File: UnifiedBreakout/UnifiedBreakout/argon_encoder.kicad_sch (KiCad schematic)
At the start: 3 parts, among them J12 ENCODER IN, J13 ENCODER OUT

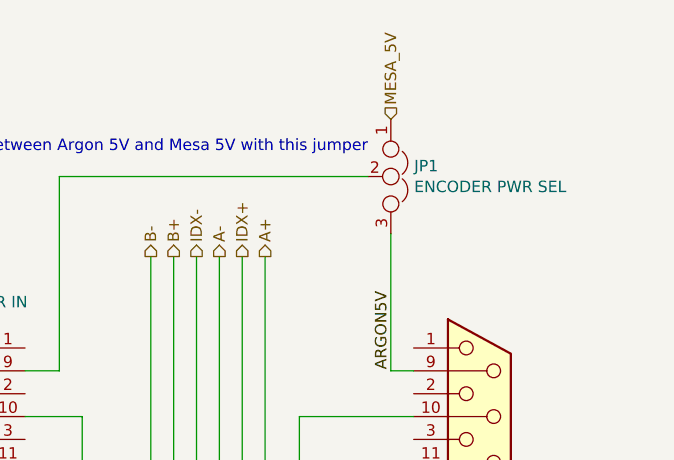
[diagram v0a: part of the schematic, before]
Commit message: Upgrade to new KiCAD version
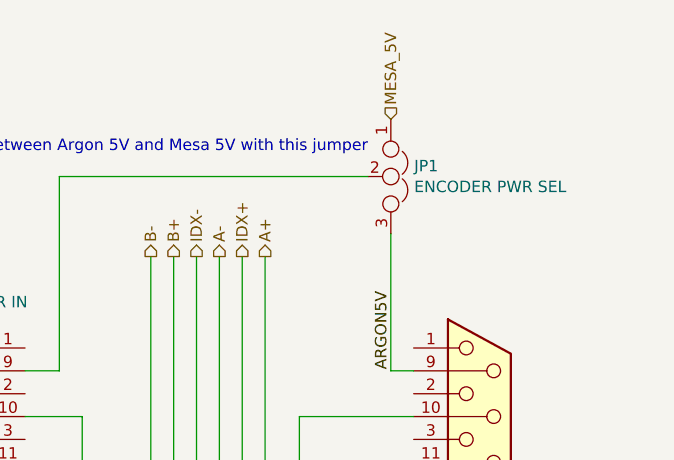
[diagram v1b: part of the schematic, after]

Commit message: WIP updating breakout for electrical enclosure
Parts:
- removed JP1: ENCODER PWR SEL, Connector_PinHeader_2.54mm:PinHeader_1x03_P2.54mm_Vertical, symbol UnifiedBreakout-rescue:Jumper_NC_Dual-Device
- J12, J13: symbol UnifiedBreakout-rescue:DB15_Female_MountingHoles-Connector -> Connector:DA15_Receptacle
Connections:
- net ARGON5V is gone; now on an unnamed net: J13.9 (P9)
- net GND: no longer J12.0 (PAD), J13.0 (PAD)
- no-connect marks 0 -> 14
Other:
- note added: "Encoder powered by Argon"
- note removed: "Select between Argon 5V and Mesa 5V with this jumper"

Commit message: Add stacked DA15 part
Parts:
- removed J12: ENCODER IN, Connector_Dsub:DSUB-15_Female_Horizontal_P2.77x2.84mm_EdgePinOffset7.70mm_Housed_MountingHolesOffset9.12mm, symbol Connector:DA15_Receptacle
- removed J13: ENCODER OUT, Connector_Dsub:DSUB-15_Female_Horizontal_P2.77x2.84mm_EdgePinOffset7.70mm_Housed_MountingHolesOffset9.12mm, symbol Connector:DA15_Receptacle
- added J3: Dual DA15 Stacked, UnifiedBreakout:NorComp-Dual-DA15, symbol UnifiedBreakout:DA15_Receptacle_Dual
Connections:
- net A+: now also J3.A8, J3.B8
- net A-: now also J3.A7, J3.B7
- net B+: now also J3.A6, J3.B6
- net B-: now also J3.A5, J3.B5
- net GND: now also J3.A10, J3.B10, J3.MH1, J3.MH2, J3.MH3, J3.MH4
- net IDX+: now also J3.A15, J3.B15
- net IDX-: now also J3.A14, J3.B14
- new net: J3.A9, J3.B9
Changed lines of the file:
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@@
   (junction (at 130.81 106.68) (diameter 0.9144) (color 0 0 0 0)
+  )
+  (junction (at 96.52 114.3) (diameter 0) (color 0 0 0 0)
   )
   (junction (at 125.73 101.6) (diameter 0.9144) (color 0 0 0 0)
@@
     (stroke (width 0) (type solid))
   )
+  (wire (pts (xy 93.98 114.3) (xy 96.52 114.3))
+    (stroke (width 0) (type default))
+  )
   (wire (pts (xy 110.49 114.3) (xy 96.52 114.3))
     (stroke (width 0) (type solid))
@@
     (stroke (width 0) (type solid))
   )
+  (wire (pts (xy 157.48 111.76) (xy 157.48 114.3))
+    (stroke (width 0) (type default))
+  )
   (wire (pts (xy 104.14 101.6) (xy 125.73 101.6))
     (stroke (width 0) (type solid))
   )
+  (wire (pts (xy 157.48 114.3) (xy 154.94 114.3))
+    (stroke (width 0) (type default))
+  )
   (wire (pts (xy 118.11 91.44) (xy 118.11 60.96))
     (stroke (width 0) (type solid))
@@
   (wire (pts (xy 147.32 104.14) (xy 128.27 104.14))
     (stroke (width 0) (type solid))
+  )
+  (wire (pts (xy 93.98 111.76) (xy 93.98 114.3))
+    (stroke (width 0) (type default))
   )
   (wire (pts (xy 104.14 78.74) (xy 110.49 78.74))
@@
     (effects (font (size 1.27 1.27)) (justify left))
   )
-  (symbol (lib_id "Connector:DA15_Receptacle") (at 154.94 88.9 0) (unit 1)
-    (in_bom yes) (on_board yes) (dnp no)
-    (property "Reference" "J13" (at 158.8516 88.8492 0)
-      (effects (font (size 1.27 1.27)) (justify left))
-    )
-    (property "Value" "ENCODER OUT" (at 158.8516 91.1606 0)
-      (effects (font (size 1.27 1.27)) (justify left))
-    )
-    (property "Footprint" "Connector_Dsub:DSUB-15_Female_Horizontal_P2.77x2.84mm_EdgePinOffset7.70mm_Housed_MountingHolesOffset9.12mm" (at 154.94 88.9 0)
+  (symbol (lib_id "UnifiedBreakout:DA15_Receptacle_Dual") (at 154.94 88.9 0) (unit 2)
+    (in_bom yes) (on_board yes) (dnp no) (fields_autoplaced)
+    (property "Reference" "J3" (at 160.02 84.455 0)
+      (effects (font (size 1.27 1.27)) (justify left))
+    )
+    (property "Value" "Dual DA15 Stacked" (at 160.02 86.995 0)
+      (effects (font (size 1.27 1.27)) (justify left))
+    )
+    (property "Footprint" "UnifiedBreakout:NorComp-Dual-DA15" (at 154.94 88.9 0)
       (effects (font (size 1.27 1.27)) hide)
     )
@@
       (effects (font (size 1.27 1.27)) hide)
     )
-    (property "Farnell PN" "" (at 154.94 88.9 0)
-      (effects (font (size 1.27 1.27)) hide)
-    )
-    (pin "1")
-    (pin "10")
-    (pin "11")
-    (pin "12")
-    (pin "13")
-    (pin "14")
-    (pin "15")
-    (pin "2")
-    (pin "3")
-    (pin "4")
-    (pin "5")
-    (pin "6")
-    (pin "7")
-    (pin "8")
-    (pin "9")
+    (property "Farnell PN" "2294319" (at 160.02 89.535 0)
+      (effects (font (size 1.27 1.27)) (justify left))
+    )
+    (property "MPN" "178-015-513R571" (at 160.02 92.075 0)
+      (effects (font (size 1.27 1.27)) (justify left))
+    )
+    (property "Manufacturer" "NORCOMP" (at 160.02 94.615 0)
+      (effects (font (size 1.27 1.27)) (justify left))
+    )
+    (pin "A1")
+    (pin "A10")
+    (pin "A11")
+    (pin "A12")
+    (pin "A13")
+    (pin "A14")
+    (pin "A15")
+    (pin "A2")
+    (pin "A3")
+    (pin "A4")
+    (pin "A5")
+    (pin "A6")
+    (pin "A7")
+    (pin "A8")
+    (pin "A9")
+    (pin "MH1")
+    (pin "MH2")
+    (pin "")
+    (pin "B1")
+    (pin "B10")
+    (pin "B11")
+    (pin "B12")
+    (pin "B13")
+    (pin "B14")
+    (pin "B15")
+    (pin "B2")
+    (pin "B3")
+    (pin "B4")
+    (pin "B5")
+    (pin "B6")
+    (pin "B7")
+    (pin "B8")
+    (pin "B9")
+    (pin "MH3")
+    (pin "MH4")
     (instances
       (project "UnifiedBreakout"
         (path "/e63e39d7-6ac0-4ffd-8aa3-1841a4541b55/00000000-0000-0000-0000-00005e9de03a"
-          (reference "J13") (unit 1)
+          (reference "J3") (unit 2)
         )
       )
     )
   )
-  (symbol (lib_id "Connector:DA15_Receptacle") (at 96.52 88.9 0) (mirror y) (unit 1)
+  (symbol (lib_id "UnifiedBreakout:DA15_Receptacle_Dual") (at 96.52 88.9 0) (mirror y) (unit 1)
     (in_bom yes) (on_board yes) (dnp no)
-    (property "Reference" "J12" (at 98.9076 63.7032 0)
-      (effects (font (size 1.27 1.27)))
-    )
-    (property "Value" "ENCODER IN" (at 98.9076 66.0146 0)
-      (effects (font (size 1.27 1.27)))
-    )
-    (property "Footprint" "Connector_Dsub:DSUB-15_Female_Horizontal_P2.77x2.84mm_EdgePinOffset7.70mm_Housed_MountingHolesOffset9.12mm" (at 96.52 88.9 0)
+    (property "Reference" "J3" (at 91.44 93.345 0)
+      (effects (font (size 1.27 1.27)) (justify left))
+    )
+    (property "Value" "Dual DA15 Stacked" (at 91.44 90.805 0)
+      (effects (font (size 1.27 1.27)) (justify left))
+    )
+    (property "Footprint" "UnifiedBreakout:NorComp-Dual-DA15" (at 96.52 88.9 0)
       (effects (font (size 1.27 1.27)) hide)
     )
@@
       (effects (font (size 1.27 1.27)) hide)
     )
-    (property "Farnell PN" "" (at 96.52 88.9 0)
-      (effects (font (size 1.27 1.27)) hide)
-    )
-    (pin "1")
-    (pin "10")
-    (pin "11")
-    (pin "12")
-    (pin "13")
-    (pin "14")
-    (pin "15")
-    (pin "2")
-    (pin "3")
-    (pin "4")
-    (pin "5")
-    (pin "6")
-    (pin "7")
-    (pin "8")
-    (pin "9")
+    (property "Farnell PN" "2294319" (at 91.44 88.265 0)
+      (effects (font (size 1.27 1.27)) (justify left))
+    )
+    (property "MPN" "178-015-513R571" (at 91.44 85.725 0)
+      (effects (font (size 1.27 1.27)) (justify left))
+    )
+    (property "Manufacturer" "NORCOMP" (at 91.44 83.185 0)
+      (effects (font (size 1.27 1.27)) (justify left))
+    )
+    (pin "A1")
+    (pin "A10")
+    (pin "A11")
+    (pin "A12")
+    (pin "A13")
+    (pin "A14")
+    (pin "A15")
+    (pin "A2")
+    (pin "A3")
+    (pin "A4")
+    (pin "A5")
+    (pin "A6")
+    (pin "A7")
+    (pin "A8")
+    (pin "A9")
+    (pin "MH1")
+    (pin "MH2")
+    (pin "")
+    (pin "B1")
+    (pin "B10")
+    (pin "B11")
+    (pin "B12")
+    (pin "B13")
+    (pin "B14")
+    (pin "B15")
+    (pin "B2")
+    (pin "B3")
+    (pin "B4")
+    (pin "B5")
+    (pin "B6")
+    (pin "B7")
+    (pin "B8")
+    (pin "B9")
+    (pin "MH3")
+    (pin "MH4")
     (instances
       (project "UnifiedBreakout"
         (path "/e63e39d7-6ac0-4ffd-8aa3-1841a4541b55/00000000-0000-0000-0000-00005e9de03a"
-          (reference "J12") (unit 1)
+          (reference "J3") (unit 1)
         )
       )

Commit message: Update IO and opto
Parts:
- renumbered J3 to J1
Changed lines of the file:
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@@
   (symbol (lib_id "UnifiedBreakout:DA15_Receptacle_Dual") (at 154.94 88.9 0) (unit 2)
     (in_bom yes) (on_board yes) (dnp no) (fields_autoplaced)
-    (property "Reference" "J3" (at 160.02 84.455 0)
+    (property "Reference" "J1" (at 160.02 84.455 0)
       (effects (font (size 1.27 1.27)) (justify left))
     )
@@
       (project "UnifiedBreakout"
         (path "/e63e39d7-6ac0-4ffd-8aa3-1841a4541b55/00000000-0000-0000-0000-00005e9de03a"
-          (reference "J3") (unit 2)
+          (reference "J1") (unit 2)
         )
       )
@@
   (symbol (lib_id "UnifiedBreakout:DA15_Receptacle_Dual") (at 96.52 88.9 0) (mirror y) (unit 1)
     (in_bom yes) (on_board yes) (dnp no)
-    (property "Reference" "J3" (at 91.44 93.345 0)
+    (property "Reference" "J1" (at 91.44 93.345 0)
       (effects (font (size 1.27 1.27)) (justify left))
     )
@@
       (project "UnifiedBreakout"
         (path "/e63e39d7-6ac0-4ffd-8aa3-1841a4541b55/00000000-0000-0000-0000-00005e9de03a"
-          (reference "J3") (unit 1)
+          (reference "J1") (unit 1)
         )
       )

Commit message: Started some layout
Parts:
- removed J1: Dual DA15 Stacked, UnifiedBreakout:NorComp-Dual-DA15, symbol UnifiedBreakout:DA15_Receptacle_Dual
- added J10, J11: DA15_Receptacle_MountingHoles, Connector_Dsub:DSUB-15_Female_Vertical_P2.77x2.84mm_MountingHoles, symbol Connector:DA15_Receptacle_MountingHoles
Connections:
- net A+: now also J10.8, J11.8
- net A-: now also J10.7, J11.7
- net B+: now also J10.6, J11.6
- net B-: now also J10.5, J11.5
- net GND: now also J10.0 (PAD), J10.10 (P10), J11.0 (PAD), J11.10 (P10)
- net IDX+: now also J10.15 (P15), J11.15 (P15)
- net IDX-: now also J10.14 (P14), J11.14 (P14)
- new net: J10.9 (P9), J11.9 (P9)
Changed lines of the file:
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@@
   (junction (at 130.81 106.68) (diameter 0.9144) (color 0 0 0 0)
-  )
-  (junction (at 96.52 114.3) (diameter 0) (color 0 0 0 0)
   )
   (junction (at 125.73 101.6) (diameter 0.9144) (color 0 0 0 0)
@@
     (stroke (width 0) (type solid))
   )
-  (wire (pts (xy 93.98 114.3) (xy 96.52 114.3))
-    (stroke (width 0) (type default))
-  )
   (wire (pts (xy 110.49 114.3) (xy 96.52 114.3))
     (stroke (width 0) (type solid))
@@
     (stroke (width 0) (type solid))
   )
-  (wire (pts (xy 157.48 111.76) (xy 157.48 114.3))
-    (stroke (width 0) (type default))
-  )
   (wire (pts (xy 104.14 101.6) (xy 125.73 101.6))
     (stroke (width 0) (type solid))
   )
-  (wire (pts (xy 157.48 114.3) (xy 154.94 114.3))
-    (stroke (width 0) (type default))
-  )
   (wire (pts (xy 118.11 91.44) (xy 118.11 60.96))
     (stroke (width 0) (type solid))
@@
   (wire (pts (xy 147.32 104.14) (xy 128.27 104.14))
     (stroke (width 0) (type solid))
-  )
-  (wire (pts (xy 93.98 111.76) (xy 93.98 114.3))
-    (stroke (width 0) (type default))
   )
   (wire (pts (xy 104.14 78.74) (xy 110.49 78.74))
@@
     (effects (font (size 1.27 1.27)) (justify left))
   )
-  (symbol (lib_id "UnifiedBreakout:DA15_Receptacle_Dual") (at 154.94 88.9 0) (unit 2)
+  (symbol (lib_id "Connector:DA15_Receptacle_MountingHoles") (at 154.94 88.9 0) (unit 1)
     (in_bom yes) (on_board yes) (dnp no) (fields_autoplaced)
-    (property "Reference" "J1" (at 160.02 84.455 0)
-      (effects (font (size 1.27 1.27)) (justify left))
-    )
-    (property "Value" "Dual DA15 Stacked" (at 160.02 86.995 0)
-      (effects (font (size 1.27 1.27)) (justify left))
-    )
-    (property "Footprint" "UnifiedBreakout:NorComp-Dual-DA15" (at 154.94 88.9 0)
+    (property "Reference" "J10" (at 160.02 88.265 0)
+      (effects (font (size 1.27 1.27)) (justify left))
+    )
+    (property "Value" "DA15_Receptacle_MountingHoles" (at 160.02 90.805 0)
+      (effects (font (size 1.27 1.27)) (justify left))
+    )
+    (property "Footprint" "Connector_Dsub:DSUB-15_Female_Vertical_P2.77x2.84mm_MountingHoles" (at 154.94 88.9 0)
       (effects (font (size 1.27 1.27)) hide)
     )
@@
       (effects (font (size 1.27 1.27)) hide)
     )
-    (property "Farnell PN" "2294319" (at 160.02 89.535 0)
-      (effects (font (size 1.27 1.27)) (justify left))
-    )
-    (property "MPN" "178-015-513R571" (at 160.02 92.075 0)
-      (effects (font (size 1.27 1.27)) (justify left))
-    )
-    (property "Manufacturer" "NORCOMP" (at 160.02 94.615 0)
-      (effects (font (size 1.27 1.27)) (justify left))
-    )
-    (pin "A1")
-    (pin "A10")
-    (pin "A11")
-    (pin "A12")
-    (pin "A13")
-    (pin "A14")
-    (pin "A15")
-    (pin "A2")
-    (pin "A3")
-    (pin "A4")
-    (pin "A5")
-    (pin "A6")
-    (pin "A7")
-    (pin "A8")
-    (pin "A9")
-    (pin "MH1")
-    (pin "MH2")
-    (pin "")
-    (pin "B1")
-    (pin "B10")
-    (pin "B11")
-    (pin "B12")
-    (pin "B13")
-    (pin "B14")
-    (pin "B15")
-    (pin "B2")
-    (pin "B3")
-    (pin "B4")
-    (pin "B5")
-    (pin "B6")
-    (pin "B7")
-    (pin "B8")
-    (pin "B9")
-    (pin "MH3")
-    (pin "MH4")
+    (property "Farnell PN" "1103914" (at 154.94 88.9 0)
+      (effects (font (size 1.27 1.27)) hide)
+    )
+    (property "MPN" "D15S24A4GV00LF " (at 154.94 88.9 0)
+      (effects (font (size 1.27 1.27)) hide)
+    )
+    (property "Manufacturer" "AMPHENOL" (at 154.94 88.9 0)
+      (effects (font (size 1.27 1.27)) hide)
+    )
+    (pin "0")
+    (pin "1")
+    (pin "10")
+    (pin "11")
+    (pin "12")
+    (pin "13")
+    (pin "14")
+    (pin "15")
+    (pin "2")
+    (pin "3")
+    (pin "4")
+    (pin "5")
+    (pin "6")
+    (pin "7")
+    (pin "8")
+    (pin "9")
     (instances
       (project "UnifiedBreakout"
         (path "/e63e39d7-6ac0-4ffd-8aa3-1841a4541b55/00000000-0000-0000-0000-00005e9de03a"
-          (reference "J1") (unit 2)
+          (reference "J10") (unit 1)
         )
       )
     )
   )
-  (symbol (lib_id "UnifiedBreakout:DA15_Receptacle_Dual") (at 96.52 88.9 0) (mirror y) (unit 1)
+  (symbol (lib_id "Connector:DA15_Receptacle_MountingHoles") (at 96.52 88.9 0) (mirror y) (unit 1)
     (in_bom yes) (on_board yes) (dnp no)
-    (property "Reference" "J1" (at 91.44 93.345 0)
-      (effects (font (size 1.27 1.27)) (justify left))
-    )
-    (property "Value" "Dual DA15 Stacked" (at 91.44 90.805 0)
-      (effects (font (size 1.27 1.27)) (justify left))
-    )
-    (property "Footprint" "UnifiedBreakout:NorComp-Dual-DA15" (at 96.52 88.9 0)
+    (property "Reference" "J11" (at 91.44 88.265 0)
+      (effects (font (size 1.27 1.27)) (justify left))
+    )
+    (property "Value" "DA15_Receptacle_MountingHoles" (at 91.44 90.805 0)
+      (effects (font (size 1.27 1.27)) (justify left))
+    )
+    (property "Footprint" "Connector_Dsub:DSUB-15_Female_Vertical_P2.77x2.84mm_MountingHoles" (at 96.52 88.9 0)
       (effects (font (size 1.27 1.27)) hide)
     )
@@
       (effects (font (size 1.27 1.27)) hide)
     )
-    (property "Farnell PN" "2294319" (at 91.44 88.265 0)
-      (effects (font (size 1.27 1.27)) (justify left))
-    )
-    (property "MPN" "178-015-513R571" (at 91.44 85.725 0)
-      (effects (font (size 1.27 1.27)) (justify left))
-    )
-    (property "Manufacturer" "NORCOMP" (at 91.44 83.185 0)
-      (effects (font (size 1.27 1.27)) (justify left))
-    )
-    (pin "A1")
-    (pin "A10")
-    (pin "A11")
-    (pin "A12")
-    (pin "A13")
-    (pin "A14")
-    (pin "A15")
-    (pin "A2")
-    (pin "A3")
-    (pin "A4")
-    (pin "A5")
-    (pin "A6")
-    (pin "A7")
-    (pin "A8")
-    (pin "A9")
-    (pin "MH1")
-    (pin "MH2")
-    (pin "")
-    (pin "B1")
-    (pin "B10")
-    (pin "B11")
-    (pin "B12")
-    (pin "B13")
-    (pin "B14")
-    (pin "B15")
-    (pin "B2")
-    (pin "B3")
-    (pin "B4")
-    (pin "B5")
-    (pin "B6")
-    (pin "B7")
-    (pin "B8")
-    (pin "B9")
-    (pin "MH3")
-    (pin "MH4")
+    (property "Farnell PN" "1103914" (at 96.52 88.9 0)
+      (effects (font (size 1.27 1.27)) hide)
+    )
+    (property "MPN" "D15S24A4GV00LF " (at 96.52 88.9 0)
+      (effects (font (size 1.27 1.27)) hide)
+    )
+    (property "Manufacturer" "AMPHENOL" (at 96.52 88.9 0)
+      (effects (font (size 1.27 1.27)) hide)
+    )
+    (pin "0")
+    (pin "1")
+    (pin "10")
+    (pin "11")
+    (pin "12")
+    (pin "13")
+    (pin "14")
+    (pin "15")
+    (pin "2")
+    (pin "3")
+    (pin "4")
+    (pin "5")
+    (pin "6")
+    (pin "7")
+    (pin "8")
+    (pin "9")
     (instances
       (project "UnifiedBreakout"
         (path "/e63e39d7-6ac0-4ffd-8aa3-1841a4541b55/00000000-0000-0000-0000-00005e9de03a"
-          (reference "J1") (unit 1)
+          (reference "J11") (unit 1)
         )
       )

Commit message: Some layout
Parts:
- renumbered J11 to J1, J10 to J2
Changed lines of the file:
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@@
   (symbol (lib_id "Connector:DA15_Receptacle_MountingHoles") (at 154.94 88.9 0) (unit 1)
     (in_bom yes) (on_board yes) (dnp no) (fields_autoplaced)
-    (property "Reference" "J10" (at 160.02 88.265 0)
+    (property "Reference" "J2" (at 160.02 88.265 0)
       (effects (font (size 1.27 1.27)) (justify left))
     )
@@
       (project "UnifiedBreakout"
         (path "/e63e39d7-6ac0-4ffd-8aa3-1841a4541b55/00000000-0000-0000-0000-00005e9de03a"
-          (reference "J10") (unit 1)
+          (reference "J2") (unit 1)
         )
       )
@@
   (symbol (lib_id "Connector:DA15_Receptacle_MountingHoles") (at 96.52 88.9 0) (mirror y) (unit 1)
     (in_bom yes) (on_board yes) (dnp no)
-    (property "Reference" "J11" (at 91.44 88.265 0)
+    (property "Reference" "J1" (at 91.44 88.265 0)
       (effects (font (size 1.27 1.27)) (justify left))
     )
@@
       (project "UnifiedBreakout"
         (path "/e63e39d7-6ac0-4ffd-8aa3-1841a4541b55/00000000-0000-0000-0000-00005e9de03a"
-          (reference "J11") (unit 1)
+          (reference "J1") (unit 1)
         )
       )
